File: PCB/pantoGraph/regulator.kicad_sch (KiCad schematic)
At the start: 3 parts, among them U6 L78L05_SOT89

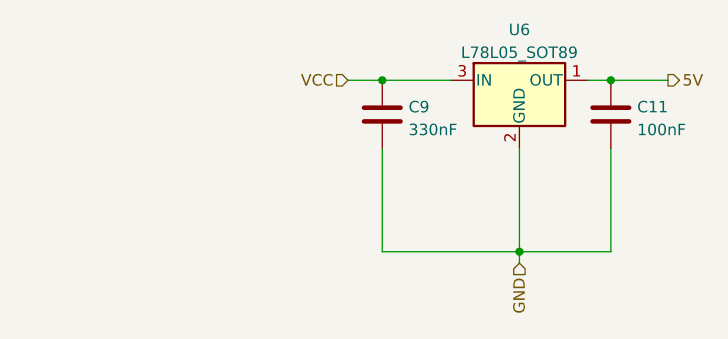
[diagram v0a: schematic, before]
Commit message: Changed OSSD code to retain aspects in EEPROM. In the event that the power has been cut-off. The OSSD can resume it's last known state. This is untested and I may want to change this into an option.
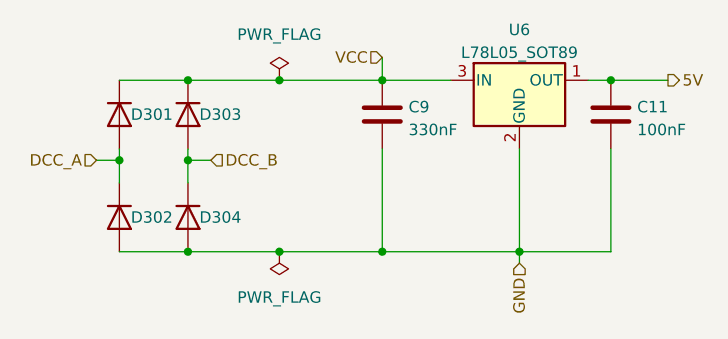
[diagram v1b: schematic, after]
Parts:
- added D301, D302, D303, D304: 1N4148WS, Diode_SMD:D_SOD-323, symbol custom_kicad_lib_sk:1N4148WS
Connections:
- net GND: now also D302.2 (A), D304.2 (A)
- net VCC: now also D301.1 (K), D303.1 (K)
- new net DCC_A: D301.2 (A), D302.1 (K)
- new net DCC_B: D303.2 (A), D304.1 (K)
